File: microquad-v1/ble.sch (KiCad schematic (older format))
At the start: 7 parts

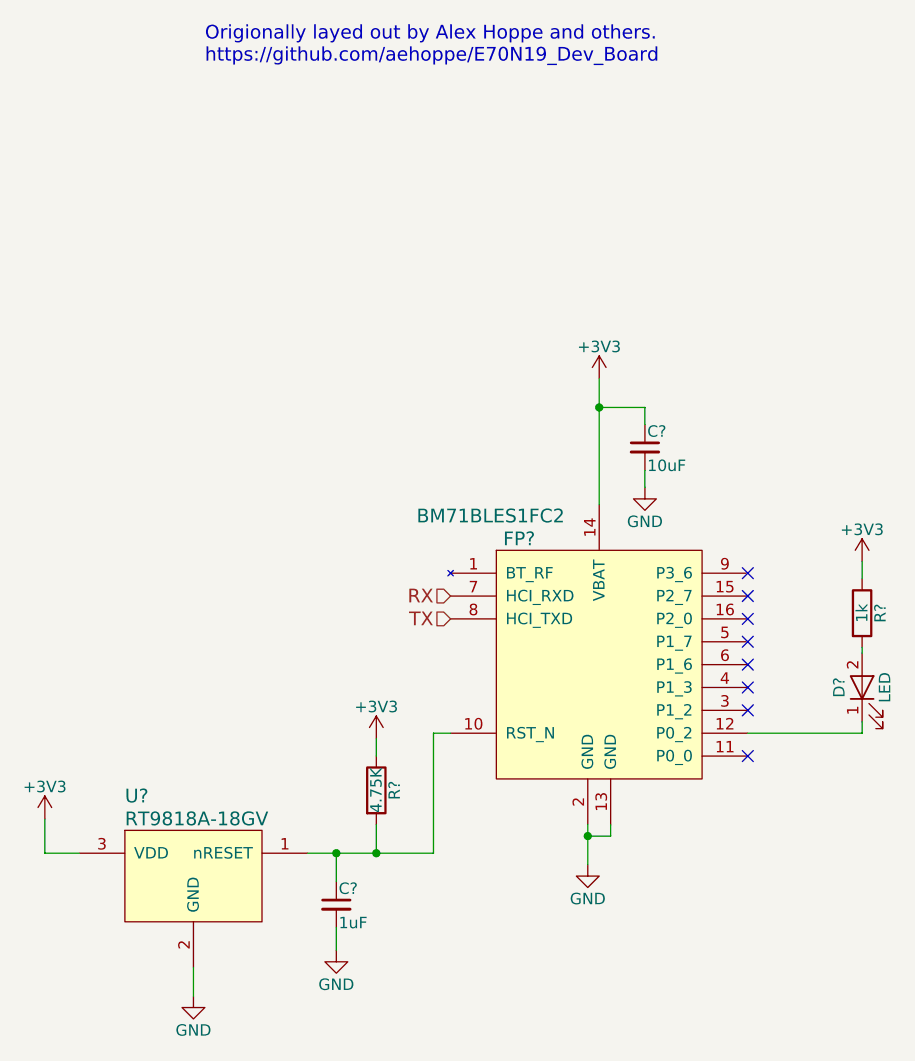
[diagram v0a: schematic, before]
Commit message: Fixed DRC errors (the ladybug is now happy)
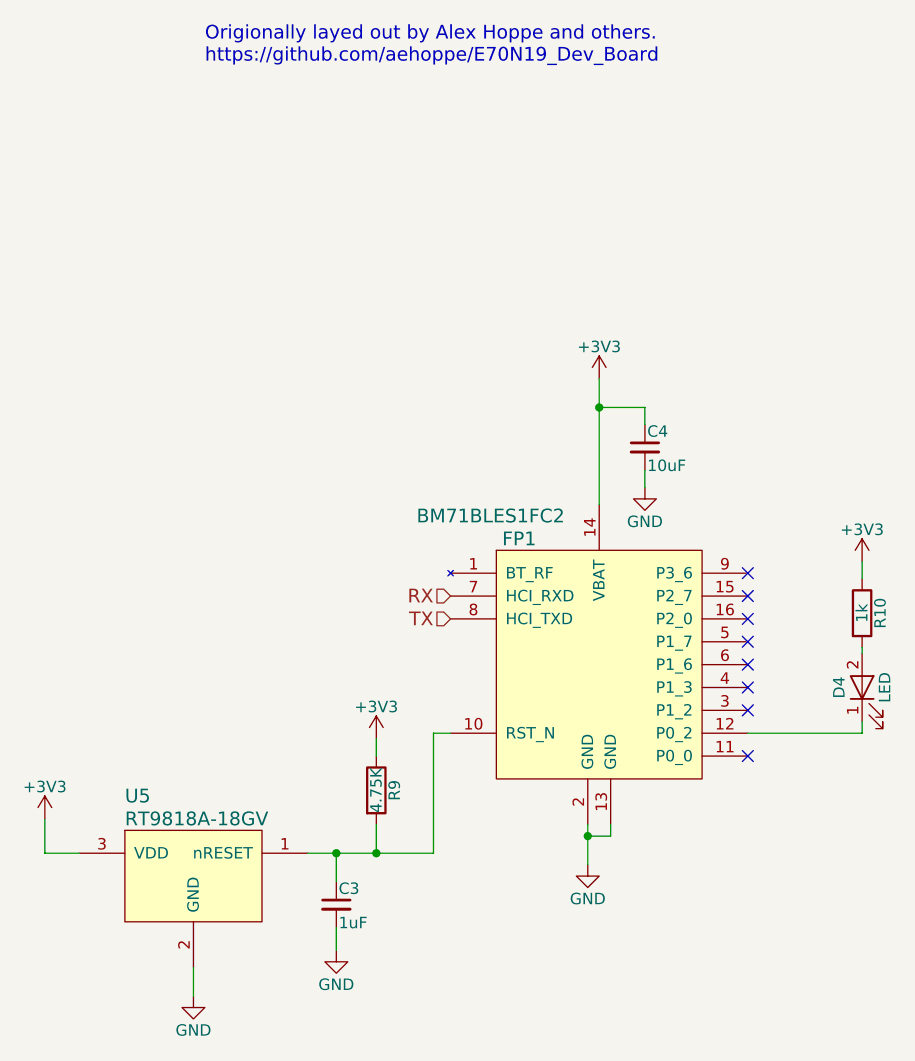
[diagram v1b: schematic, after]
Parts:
- gave numbers to parts that had none: 7
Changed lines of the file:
@@
 $Descr A4 11693 8268
 encoding utf-8
-Sheet 6 9
+Sheet 9 9
 Title ""
 Date ""
@@
 $EndDescr
 $Comp
-L BM71BLES1FC2 FP?
+L BM71BLES1FC2 FP1
 U 1 1 59F5B047
 P 6000 3350
-F 0 "FP?" H 5650 3900 60  0000 C CNN
+F 0 "FP1" H 5650 3900 60  0000 C CNN
 F 1 "BM71BLES1FC2" H 5525 4000 60  0000 C CNN
 F 2 "eclectronics:BM71BLES1FC2" H 6000 2850 60  0001 C CNN
@@
 $EndComp
 $Comp
-L RT9818A-18GV U?
+L RT9818A-18GV U5
 U 1 1 59F5B04E
 P 4225 4275
-F 0 "U?" H 3925 4625 60  0000 L CNN
+F 0 "U5" H 3925 4625 60  0000 L CNN
 F 1 "RT9818A-18GV" H 3925 4525 60  0000 L CNN
 F 2 "TO_SOT_Packages_SMD:SOT-23" H 4175 4275 60  0001 C CNN
@@
 	4725 4175 5275 4175
 $Comp
-L GND #PWR?
+L GND #PWR046
 U 1 1 59F5B056
 P 5950 4225
-F 0 "#PWR?" H 5950 3975 50  0001 C CNN
+F 0 "#PWR046" H 5950 3975 50  0001 C CNN
 F 1 "GND" H 5950 4075 50  0000 C CNN
 F 2 "" H 5950 4225 50  0001 C CNN
@@
 $EndComp
 $Comp
-L GND #PWR?
+L GND #PWR047
 U 1 1 59F5B05C
 P 4225 4800
-F 0 "#PWR?" H 4225 4550 50  0001 C CNN
+F 0 "#PWR047" H 4225 4550 50  0001 C CNN
 F 1 "GND" H 4225 4650 50  0000 C CNN
 F 2 "" H 4225 4800 50  0001 C CNN
@@
 $EndComp
 $Comp
-L R R?
+L R R9
 U 1 1 59F5B063
 P 5025 3900
-F 0 "R?" V 5105 3900 50  0000 C CNN
+F 0 "R9" V 5105 3900 50  0000 C CNN
 F 1 "4.75K" V 5025 3900 50  0000 C CNN
 F 2 "Resistors_SMD:R_0603" V 4955 3900 50  0001 C CNN
@@
 $EndComp
 $Comp
-L C_Small C?
+L C_Small C3
 U 1 1 59F5B06B
 P 4850 4400
-F 0 "C?" H 4860 4470 50  0000 L CNN
+F 0 "C3" H 4860 4470 50  0000 L CNN
 F 1 "1uF" H 4860 4320 50  0000 L CNN
 F 2 "Capacitors_SMD:C_0603" H 4850 4400 50  0001 C CNN
@@
 $EndComp
 $Comp
-L GND #PWR?
+L GND #PWR048
 U 1 1 59F5B072
 P 4850 4600
-F 0 "#PWR?" H 4850 4350 50  0001 C CNN
+F 0 "#PWR048" H 4850 4350 50  0001 C CNN
 F 1 "GND" H 4850 4450 50  0000 C CNN
 F 2 "" H 4850 4600 50  0001 C CNN
@@
 NoConn ~ 6650 3750
 $Comp
-L C_Small C?
+L C_Small C4
 U 1 1 59F5B0A2
 P 6200 2400
-F 0 "C?" H 6210 2470 50  0000 L CNN
+F 0 "C4" H 6210 2470 50  0000 L CNN
 F 1 "10uF" H 6210 2320 50  0000 L CNN
 F 2 "Capacitors_SMD:C_0805" H 6200 2400 50  0001 C CNN
@@
 Connection ~ 6000 2225
 $Comp
-L GND #PWR?
+L GND #PWR049
 U 1 1 59F5B0AC
 P 6200 2575
-F 0 "#PWR?" H 6200 2325 50  0001 C CNN
+F 0 "#PWR049" H 6200 2325 50  0001 C CNN
 F 1 "GND" H 6200 2425 50  0000 C CNN
 F 2 "" H 6200 2575 50  0001 C CNN
@@
 	6200 2500 6200 2575
 $Comp
-L R R?
+L R R10
 U 1 1 59F5B0B4
 P 7150 3125
-F 0 "R?" V 7230 3125 50  0000 C CNN
+F 0 "R10" V 7230 3125 50  0000 C CNN
 F 1 "1k" V 7150 3125 50  0000 C CNN
 F 2 "Resistors_SMD:R_0603" V 7080 3125 50  0001 C CNN
@@
 TX
 $Comp
-L +3V3 #PWR?
+L +3V3 #PWR050
 U 1 1 59F5C114
 P 6000 2100
-F 0 "#PWR?" H 6000 1950 50  0001 C CNN
+F 0 "#PWR050" H 6000 1950 50  0001 C CNN
 F 1 "+3V3" H 6000 2240 50  0000 C CNN
 F 2 "" H 6000 2100 50  0001 C CNN
@@
 	6000 2650 6000 2100
 $Comp
-L +3V3 #PWR?
+L +3V3 #PWR051
 U 1 1 59F5C188
 P 5025 3675
-F 0 "#PWR?" H 5025 3525 50  0001 C CNN
+F 0 "#PWR051" H 5025 3525 50  0001 C CNN
 F 1 "+3V3" H 5025 3815 50  0000 C CNN
 F 2 "" H 5025 3675 50  0001 C CNN
@@
 $EndComp
 $Comp
-L +3V3 #PWR?
+L +3V3 #PWR052
 U 1 1 59F5C240
 P 3575 4025
-F 0 "#PWR?" H 3575 3875 50  0001 C CNN
+F 0 "#PWR052" H 3575 3875 50  0001 C CNN
 F 1 "+3V3" H 3575 4165 50  0000 C CNN
 F 2 "" H 3575 4025 50  0001 C CNN
@@
 $EndComp
 $Comp
-L +3V3 #PWR?
+L +3V3 #PWR053
 U 1 1 59F5C2DF
 P 7150 2900
-F 0 "#PWR?" H 7150 2750 50  0001 C CNN
+F 0 "#PWR053" H 7150 2750 50  0001 C CNN
 F 1 "+3V3" H 7150 3040 50  0000 C CNN
 F 2 "" H 7150 2900 50  0001 C CNN
@@
 Origionally layed out by Alex Hoppe and others.\nhttps://github.com/aehoppe/E70N19_Dev_Board
 $Comp
-L LED D?
+L LED D4
 U 1 1 59F5C863
 P 7150 3450
-F 0 "D?" H 7150 3550 50  0000 C CNN
+F 0 "D4" H 7150 3550 50  0000 C CNN
 F 1 "LED" H 7150 3350 50  0000 C CNN
 F 2 "" H 7150 3450 50  0001 C CNN
